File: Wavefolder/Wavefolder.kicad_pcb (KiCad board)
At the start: 2 copper layers, 28 x 110 mm, 89 parts, among them J1 CV_in, J2 input, J3 Bus_i, J4 Bus_o, J5 fold, J6 pulse, J7 POWER, Q1 MMBT3904, Q2 MMBT3904, U1 TL074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

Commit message: rev1 updates
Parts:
- removed R22: 510R, Resistor_SMD:R_0805_2012Metric
- removed REF**: OSHW-Logo2_9.8x8mm_SilkScreen, Symbol:OSHW-Logo2_9.8x8mm_SilkScreen
- added C14: 470pF, Capacitor_SMD:C_0805_2012Metric, F.Cu at (-6.22, -40.0)
- moved D3 4.03 mm to (-4.10, -69.7), turned to 270 degrees
- moved D4 3.72 mm to (-3.75, -51.2), turned to 270 degrees
- moved D9 2.58 mm to (-23.8, -61.1), turned to 180 degrees
- moved R4 2.41 mm to (-21.8, -93.3)
- moved D10 2.36 mm to (-24.2, -43.0), turned to 180 degrees
- moved R21 1.88 mm to (-21.8, -95.4)
- moved R38 1.80 mm to (-24.2, -40.0), turned to 0 degrees
- moved R36 1.49 mm to (-23.8, -58.1), turned to 0 degrees
- moved C2 0.50 mm to (-25.3, -98.2)
- moved R3 0.50 mm to (-6.00, -87.0)
- moved R5 0.50 mm to (-8.25, -82.8)
- moved R7 0.50 mm to (-8.25, -84.8)
- moved R8 0.50 mm to (-9.00, -87.8)
- moved C10 0.48 mm to (-18.5, -25.7)
- moved C3 0.35 mm to (-8.47, -90.5)
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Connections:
- D13 pad 2: Net-(D13-Pad2) -> postfold
- D14 pad 1: Net-(D13-Pad2) -> postfold
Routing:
- net +12V: track 165.7 -> 156.5 mm, vias 9 -> 0
- net Net-(J3-Pad3): track 22.4 -> 30.0 mm, vias 0 -> 1
- net postfold: track 23.7 -> 17.1 mm, vias 0 -> 1
- net Net-(D13-Pad2): track 5.49 -> 0.00 mm
- net Net-(C14-Pad2): track 12.6 -> 17.3 mm
- net Net-(J1-PadT): track 56.0 -> 60.6 mm
- net prefold: track 34.0 -> 38.4 mm
- net Net-(R13-Pad2): track 13.4 -> 17.8 mm, vias 0 -> 2
- net Net-(J2-PadT): track 86.0 -> 90.0 mm, vias 0 -> 2
- net GND: track 43.6 -> 39.9 mm, vias 26 -> 28
- net Net-(J3-Pad1): track 24.5 -> 28.0 mm, vias 0 -> 1
- net CV_in: track 30.4 -> 34.0 mm, vias 0 -> 1
- net Net-(J5-PadT): track 14.2 -> 17.4 mm
- net Net-(D10-Pad3): track 8.85 -> 11.8 mm
- net Net-(D9-Pad3): track 8.85 -> 11.3 mm
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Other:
- net class Power: trace_width 0.9 -> 0.6
- board text added: "REV1"

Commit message: rev 2 changes, see revision_log
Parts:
- removed D14: 4148, Diode_THT:D_DO-35_SOD27_P7.62mm_Horizontal
- removed J3: Bus_i, Connector_PinHeader_2.54mm:PinHeader_1x04_P2.54mm_Vertical
- removed J4: Bus_o, Connector_PinHeader_2.54mm:PinHeader_1x04_P2.54mm_Vertical
- D1: footprint Diode_THT:D_DO-35_SOD27_P7.62mm_Horizontal -> Diode_SMD:D_SOD-123
- D13: value 4148 -> BAV99; footprint Diode_THT:D_DO-35_SOD27_P7.62mm_Horizontal -> Package_TO_SOT_SMD:SOT-23
- moved D1 4.19 mm to (-25.0, -90.9)
- moved D13 2.62 mm to (-11.4, -37.1)
- moved R4 2.16 mm to (-21.8, -91.2)
- moved R20 2.00 mm to (-21.8, -93.2)
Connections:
- D13 pad 2: postfold -> Net-(C14-Pad2)
- J1 pad TN: CV_in -> GND
- J2 pad TN: TRI_in -> GND
- J5 pad TN: fold_out -> Net-(J5-PadTN)
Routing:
- net CV_in: track 34.0 -> 0.00 mm, vias 1 -> 0
- net fold_out: track 30.3 -> 0.00 mm, vias 1 -> 0
- net Net-(J3-Pad3): track 30.0 -> 0.00 mm, vias 1 -> 0
- net Net-(J3-Pad1): track 28.0 -> 0.00 mm, vias 1 -> 0
- net TRI_in: track 11.4 -> 0.00 mm
- net postfold: track 17.1 -> 26.5 mm, vias 1 -> 2
- net Net-(J5-PadT): track 17.4 -> 13.8 mm, vias 2 -> 0
- net Net-(C14-Pad2): track 17.3 -> 16.4 mm
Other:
- board text removed: "CV"
- board text removed: "F"
- board text removed: "IN"
- board text removed: "OUT"
- board text removed: "REV1"
- board text removed: "T"
- board text removed: "THRU"
- board text removed: "TRI"

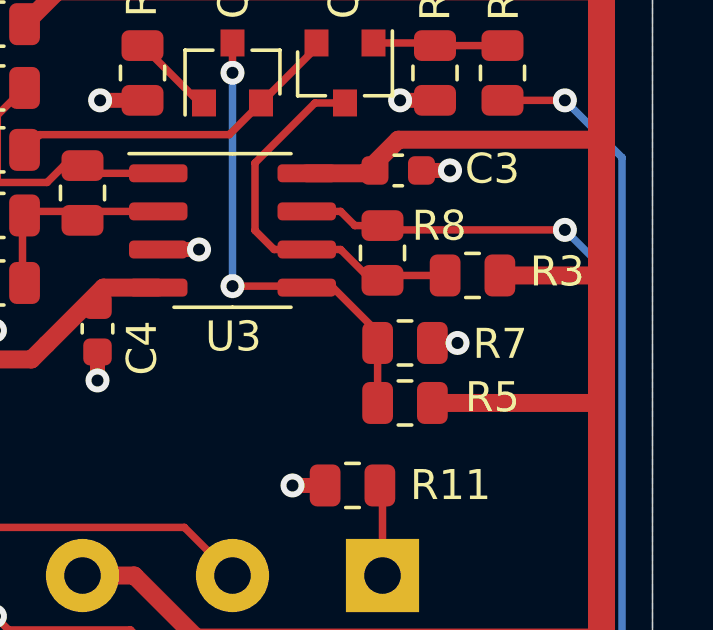
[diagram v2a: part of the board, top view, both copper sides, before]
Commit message: added VCA stability cap
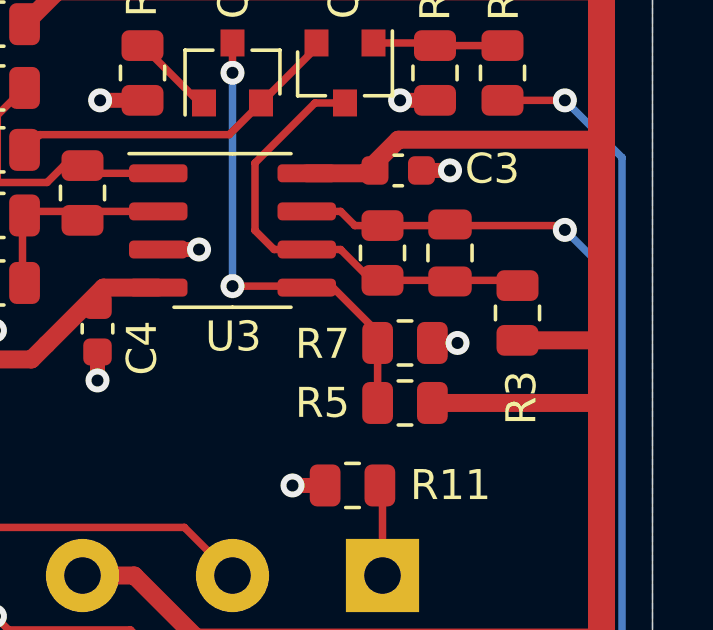
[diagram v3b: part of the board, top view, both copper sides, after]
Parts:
- added C15: 100pF, Capacitor_SMD:C_0805_2012Metric, F.Cu at (-6.75, -87.8)
- moved R3 1.95 mm to (-4.50, -85.8), turned to 90 degrees
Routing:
- net Net-(C15-Pad2): track 13.2 -> 15.7 mm
- net +12V: track 156.5 -> 155.9 mm

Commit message: rev 3 updates, see revision log
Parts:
- removed Q2: MMBT3904, Package_TO_SOT_SMD:SOT-23
- removed R11: 20K, Resistor_SMD:R_0805_2012Metric
- added RV3: 2KT, user-main:TRIM_3296W, F.Cu at (-5.03, -75.5)
- D2: footprint user-footprints:LED_3mm -> LED_THT:LED_D3.0mm
- J1, J2, J5, J6: footprint user-footprints:AudioJack_QuPing_Pushfit -> user-main:AudioJack_QingPu_WQP-PJ301BM_Vertical
- Q1: value MMBT3904 -> BC847BS; footprint Package_TO_SOT_SMD:SOT-23 -> Package_TO_SOT_SMD:SOT-363_SC-70-6
- R3, R5: value 10K -> 9.1K
- RV1, RV2: footprint user-footprints:POT_16mm_detailed -> user-clutter:POT_16mm_detailed
- moved R6 7.50 mm to (-9.50, -93.8)
- moved Q1 4.32 mm to (-14.5, -93.0), turned to 180 degrees
- moved C9 1.85 mm to (-8.75, -32.9)
- moved R10 1.85 mm to (-20.8, -31.6)
- moved R14 1.85 mm to (-18.8, -31.6)
- moved R15 1.85 mm to (-9.25, -30.4)
- moved R17 1.85 mm to (-14.8, -25.4)
- moved R18 1.85 mm to (-19.8, -34.9)
- moved R19 1.85 mm to (-19.8, -36.9)
- moved R9 1.85 mm to (-7.25, -30.4)
- moved U4 1.85 mm to (-14.0, -30.4)
- moved C10 1.85 mm to (-18.5, -27.6)
- moved D2 1.28 mm to (-24.0, -82.8), turned to -90 degrees
- moved R5 0.79 mm to (-9.02, -82.5)
- moved R7 0.79 mm to (-9.02, -84.5)
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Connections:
- J5 pad TN: Net-(J5-PadTN) -> unconnected-(J5-PadTN)
- J6 pad TN: Net-(J6-PadTN) -> unconnected-(J6-PadTN)
- Q1 pad 1: Net-(Q1-Pad1) -> Net-(R4-Pad1)
- Q1 pad 2: Net-(Q1-Pad2) -> Net-(R6-Pad1)
- R1 pad 1: Net-(Q1-Pad1) -> Net-(R1-Pad1)
- R2 pad 1: Net-(Q1-Pad1) -> Net-(R1-Pad1)
- R3 pad 1: +12V -> Net-(R3-Pad1)
- R4 pad 1: Net-(Q1-Pad2) -> Net-(R4-Pad1)
- R5 pad 1: +12V -> Net-(R5-Pad1)
- R5 pad 2: Net-(Q2-Pad3) -> Net-(R5-Pad2)
- R6 pad 1: Net-(Q2-Pad1) -> Net-(R6-Pad1)
- R7 pad 1: Net-(Q2-Pad3) -> Net-(R5-Pad2)
- RV2 pad 1: Net-(R11-Pad2) -> GND
- U3 pad 5: Net-(Q2-Pad3) -> Net-(R5-Pad2)
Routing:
- net Net-(Q2-Pad3): track 15.9 -> 0.00 mm, vias 2 -> 0
- net Net-(R1-Pad1): track 0.00 -> 15.8 mm, vias 0 -> 2
- net Net-(R5-Pad2): track 0.00 -> 13.2 mm
- net Net-(Q1-Pad2): track 11.3 -> 0.00 mm
- net Net-(R4-Pad1): track 0.00 -> 9.26 mm
- net +12V: track 155.9 -> 147.6 mm
- net Net-(R5-Pad1): track 0.00 -> 7.84 mm
- net Net-(R6-Pad1): track 0.00 -> 5.84 mm, vias 0 -> 2
- net Net-(Q1-Pad1): track 4.34 -> 0.00 mm
- net Net-(R3-Pad1): track 0.00 -> 3.55 mm
- net Net-(R11-Pad2): track 3.04 -> 0.00 mm
- net Net-(Q2-Pad1): track 2.84 -> 0.00 mm
- net Net-(J5-PadT): track 13.8 -> 16.0 mm
- net postfold: track 26.5 -> 24.7 mm
- net -12V: track 118.1 -> 116.4 mm
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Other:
- net class Default removed
- net class Power removed
- board text added: "2K"
- board text added: "LONG LEAD"
- board text added: "V1.3"
